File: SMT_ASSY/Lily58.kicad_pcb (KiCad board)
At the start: 2 copper layers, 142.5 x 106.3 mm, 86 parts, among them J0 USB_B_Micro, J2 4PIN, P1 i2c_pin, P2 i2c_pin, P3 ICSP, P4 OLED, SW1 SW_PUSH, SW10 SW_PUSH, SW11 SW_PUSH, SW12 SW_PUSH, SW13 SW_PUSH, SW14 SW_PUSH, SW15 SW_PUSH, SW16 SW_PUSH, SW17 SW_PUSH, SW18 SW_PUSH, SW19 SW_PUSH, SW2 SW_PUSH, SW20 SW_PUSH, SW21 SW_PUSH, SW22 SW_PUSH, SW23 SW_PUSH, SW24 SW_PUSH, SW25 SW_PUSH, SW26 SW_PUSH, SW27 SW_PUSH, SW28 SW_PUSH, SW29 SW_PUSH, SW3 SW_PUSH, SW4 SW_PUSH, SW5 SW_PUSH, SW6 SW_PUSH, SW7 SW_PUSH, SW8 SW_PUSH, SW9 SW_PUSH, U0 USBLC6-2SC6, U1 ProMicro, U2 ATmega32U4-AU

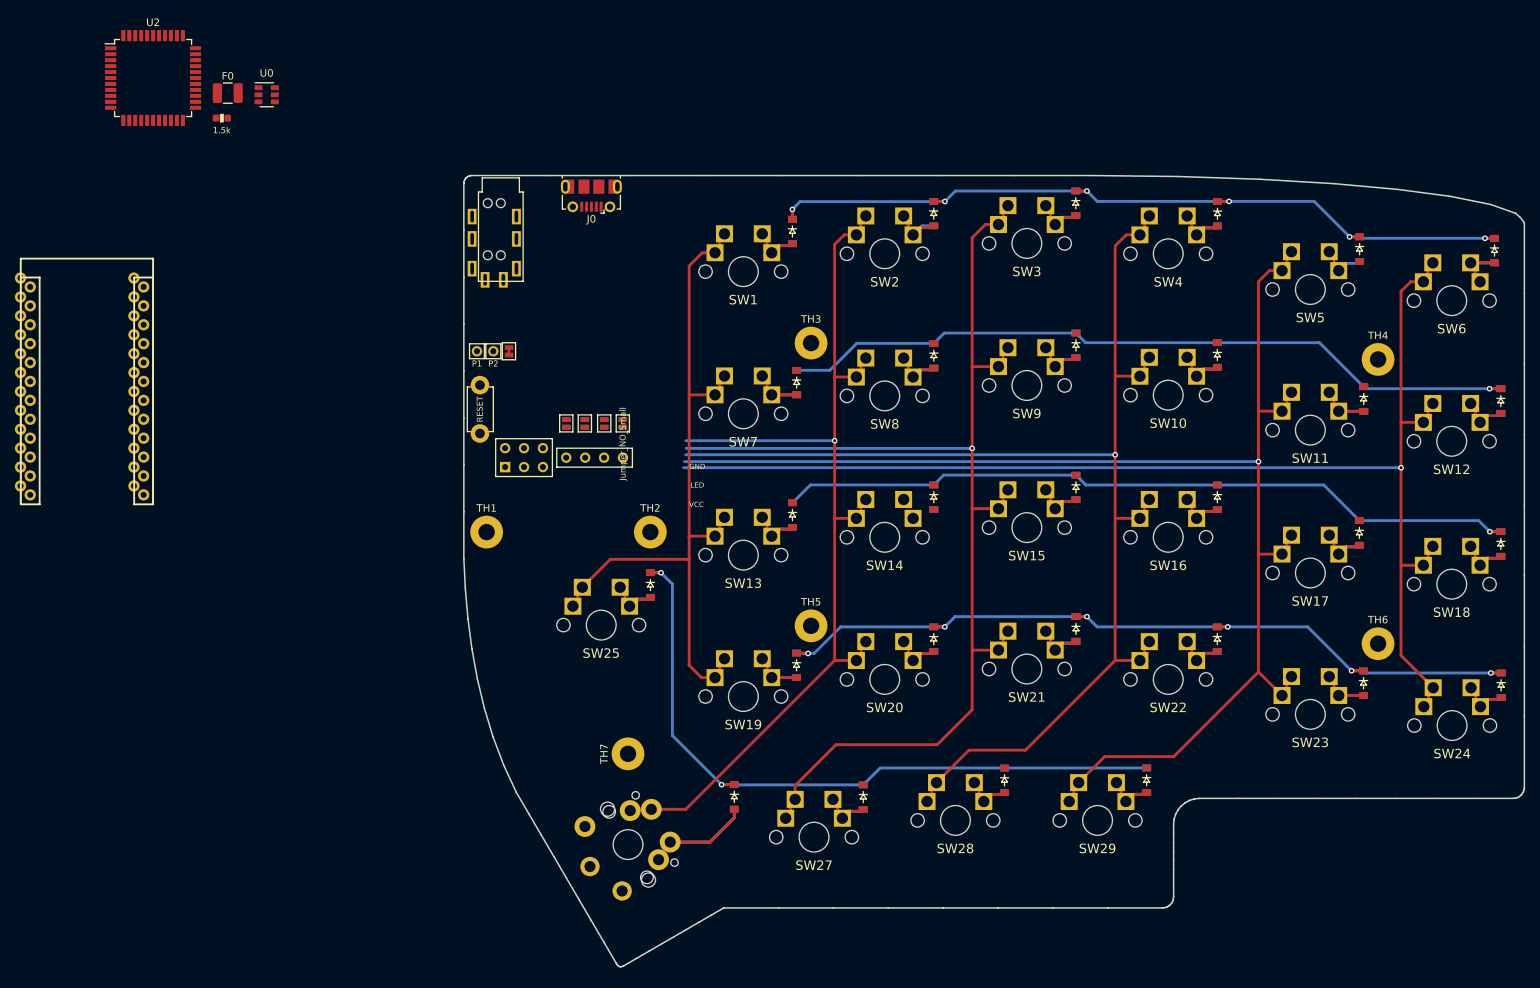
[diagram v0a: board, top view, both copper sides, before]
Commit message: Updated layout to use more comps
Need to do ATMEGA32U4 circuitry still
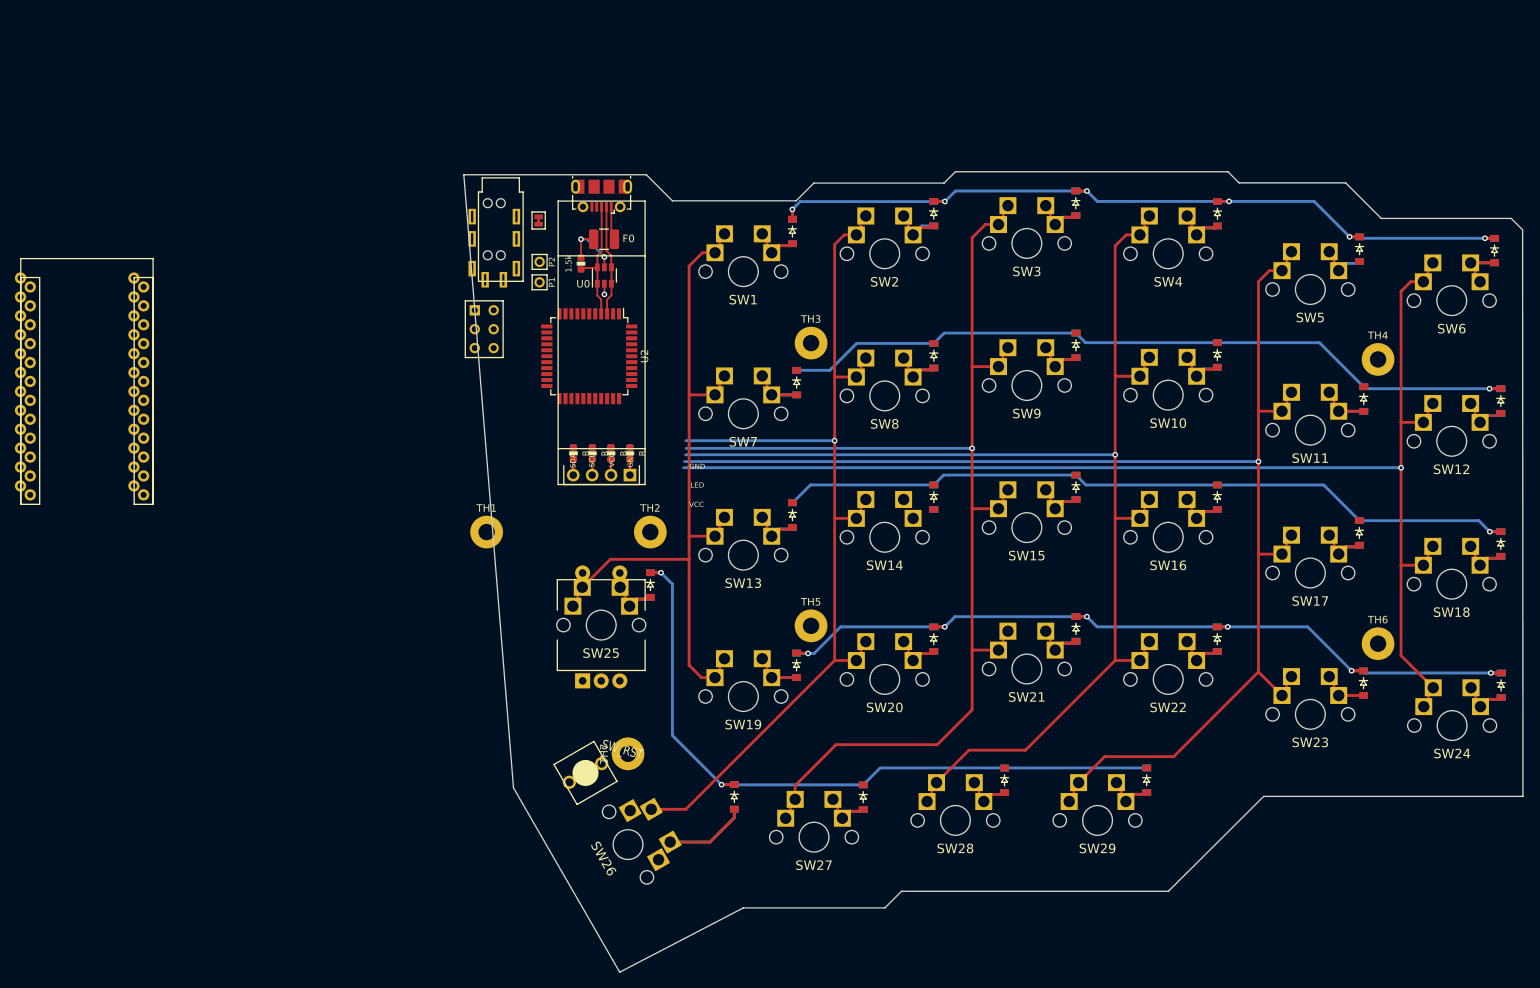
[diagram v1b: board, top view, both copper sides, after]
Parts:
- removed JP1, JP2, JP3, JP4, JP5, JP6, JP7, JP8: Jumper_NO_Small, Lily58-footprint:Jumper
- removed P4: OLED, Lily58-footprint:MY_SIL-4
- added DISP0: OLED_128x32, Keyboard_Footprints:OLED_128x32, F.Cu at (101.5, 77.3)
- added SHT1: R, Keyboard_Footprints:C_0603, F.Cu at (97.7, 74.4)
- added SHT2: R, Keyboard_Footprints:C_0603, B.Cu at (97.7, 74.4)
- added SHT3: R, Keyboard_Footprints:C_0603, F.Cu at (100.2, 74.4)
- added SHT4: R, Keyboard_Footprints:C_0603, B.Cu at (100.2, 74.4)
- added SHT5: R, Keyboard_Footprints:C_0603, F.Cu at (102.7, 74.4)
- added SHT6: R, Keyboard_Footprints:C_0603, B.Cu at (102.7, 74.4)
- added SHT7: R, Keyboard_Footprints:C_0603, F.Cu at (105.3, 74.4)
- added SHT8: R, Keyboard_Footprints:C_0603, B.Cu at (105.3, 74.4)
- added SW30: Rotary_Encoder_Switch, Keyboard_Footprints:EC11E, F.Cu at (101.4, 97.5)
- RSW1: footprint Lily58-footprint:TACT_SWITCH_TVBP06 -> Keyboard_Footprints:SPST_FSM2JRT
- SW26: footprint Lily58-footprint:MX_PG1350-Under_FLIP_HOLES_27mm -> Keyboard_Footprints:MX_1.5U_Flip
- moved U2 69.5 mm to (99.8, 61.4), turned to 270 degrees
- moved F0 54.2 mm to (101.8, 45.6)
- moved R0 52.1 mm to (98.7, 48.9), turned to 270 degrees
- moved U0 51.5 mm to (101.8, 50.5), turned to 90 degrees
- moved RSW1 50.9 mm to (99.3, 117.4), turned to 30 degrees
- moved P3 18.1 mm to (85.7, 57.7), turned to 0 degrees
- moved W1 18.0 mm to (93.0, 43.1)
- moved P2 13.5 mm to (93.1, 48.7), turned to 270 degrees
- moved P1 12.5 mm to (93.1, 51.4), turned to 270 degrees
- moved J0 1.37 mm to (101.5, 39.8)
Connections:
- U2 pad 3: (no net) -> USB_D-
- U2 pad 4: (no net) -> USB_D+
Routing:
- net USB_D+: track 0.00 -> 17.2 mm
- net USB_D-: track 0.00 -> 15.0 mm
- net VCC: track 0.00 -> 9.72 mm, vias 0 -> 2
- net VBUS: track 0.00 -> 4.54 mm
- net Net-(DISP0-Pad4): track 0.00 -> 4.27 mm
- net Net-(DISP0-Pad1): track 0.00 -> 4.17 mm
- net Net-(DISP0-Pad2): track 0.00 -> 4.17 mm
- net Net-(DISP0-Pad3): track 0.00 -> 4.14 mm
- net GND: track 0.00 -> 1.44 mm, vias 0 -> 1
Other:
- board size 142.5 x 106.3 mm -> 142.3 x 107.6 mm
